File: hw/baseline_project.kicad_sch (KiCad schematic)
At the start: 20 parts, among them J101 EXT_3V3, Q101 IRLD024PBF, SW101 UP, SW102 DOWN, SW103 LEFT, SW104 RIGHT, SW105 MODE, U101 EK-TM4C123GXL, U102 ESP8266-1, U103 Adafruit ST7735R

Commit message: hw changes
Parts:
- added 12k, 18k, 6k: R_0.125W, ECE445L:R_Axial_DIN0204_L3.6mm_D1.6mm_P7.62mm_Horizontal, symbol ECE445L:R_0.125W
- added D1: 1V0, Diode_THT:D_5W_P12.70mm_Horizontal, symbol Device:D_Small
- added LS1: Speaker, Connector_PinHeader_2.54mm:PinHeader_1x02_P2.54mm_Vertical, symbol Device:Speaker
- added Q1: IRLD024PBF, ECE445L:DIP920W60P254L490H457Q4N, symbol ECE445L:IRLD024PBF
- added R1, R2, R3, R4: 1k, ECE445L:R_Axial_DIN0204_L3.6mm_D1.6mm_P7.62mm_Horizontal, symbol ECE445L:R_0.125W
- added R5: 10k, ECE445L:R_Axial_DIN0204_L3.6mm_D1.6mm_P7.62mm_Horizontal, symbol ECE445L:R_0.125W
- added SW1: UP, ECE445L:SW_PUSH_6mm, symbol ECE445L:SW_Push
- added SW2: LEFT, ECE445L:SW_PUSH_6mm, symbol ECE445L:SW_Push
- added SW3: RIGHT, ECE445L:SW_PUSH_6mm, symbol ECE445L:SW_Push
- added SW4: DOWN, ECE445L:SW_PUSH_6mm, symbol ECE445L:SW_Push
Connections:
- net +3V3: now also D1.1 (K), LS1.1
- net GND: now also Q1.4 (S), R1.2, R2.2, R3.2, R4.2
- net PB0: now also 6k.1
- net PB1: now also 12k.1
- net PB2: now also 18k.1
- net PC4: now also R1.1, SW1.2
- net PC5: now also R4.1, SW4.2
- net PC6: now also R3.1, SW3.2
- net PC7: now also R2.1, SW2.2
- new net: 12k.2, 18k.2, 6k.2, R5.1
- new net: Q1.3 (G), R5.2
- new net: D1.2 (A), LS1.2, Q1.1 (D), Q1.2 (D)
- new net +3.3V: SW1.1, SW2.1, SW3.1, SW4.1

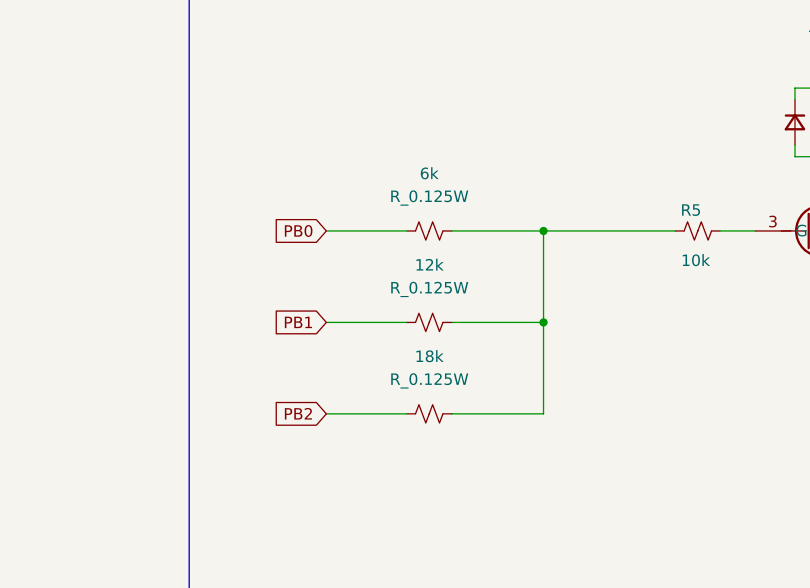
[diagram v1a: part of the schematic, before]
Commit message: lab 3 prep - tested switches, LCD and timer
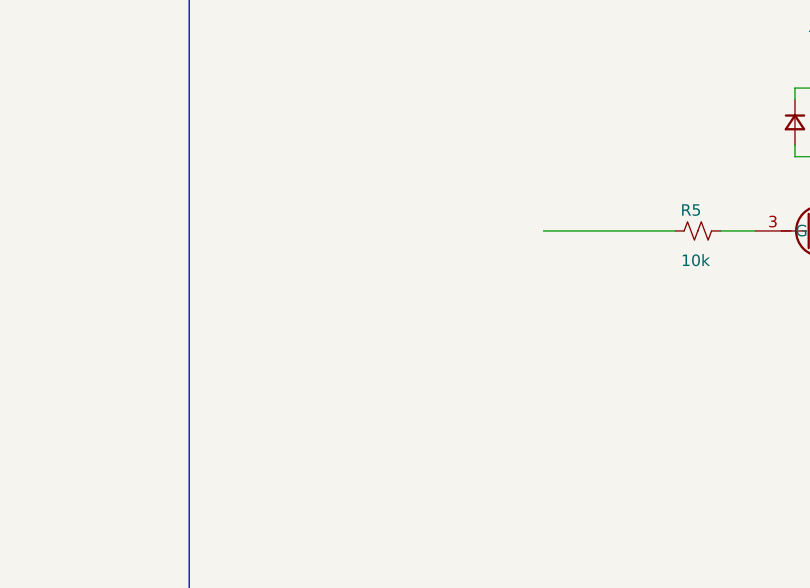
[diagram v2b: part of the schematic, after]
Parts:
- removed 12k, 18k, 6k: R_0.125W, ECE445L:R_Axial_DIN0204_L3.6mm_D1.6mm_P7.62mm_Horizontal, symbol ECE445L:R_0.125W
